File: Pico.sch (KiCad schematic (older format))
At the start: 5 parts, among them SW3001 SWITCH TACTILE SPST-NO 50MA 1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, U3001 Pico-JER

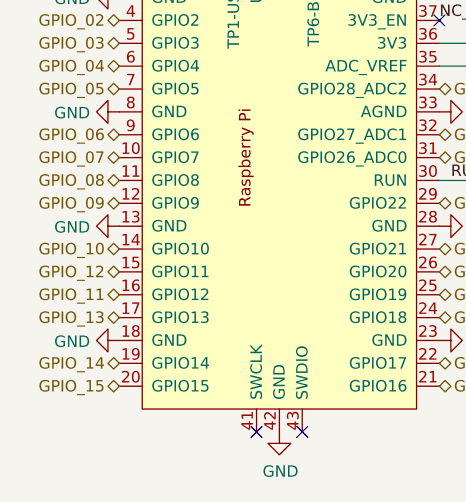
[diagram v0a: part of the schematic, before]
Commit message: Assignments for Pico GPIO 11 and 12 were flipped. Fixed.
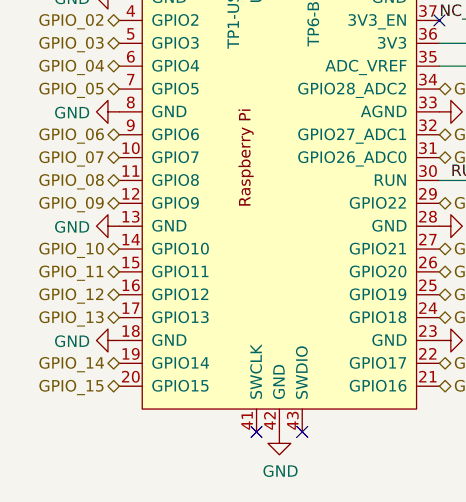
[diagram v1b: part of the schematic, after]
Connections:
- net GPIO_11: now also U3001.15 (GPIO11); no longer U3001.16 (GPIO12)
- net GPIO_12: now also U3001.16 (GPIO12); no longer U3001.15 (GPIO11)
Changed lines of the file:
@@
 GPIO_10
 Text HLabel 4900 4050 0    50   BiDi ~ 0
-GPIO_12
-Text HLabel 4900 4150 0    50   BiDi ~ 0
 GPIO_11
 Text HLabel 4900 4250 0    50   BiDi ~ 0
@@
 Text Label 6350 3650 0    50   ~ 0
 RUN_SW
+Text HLabel 4900 4150 0    50   BiDi ~ 0
+GPIO_12
 $EndSCHEMATC

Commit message: Use GP25_LED for ePaper RESET
Note: This replaces R6/196a722 in its entirety.

IS: J2901 (Connector for epaper) Pin 10 (Reset) connected to +3.3V via R2902 (100k ohm)
SHOULD BE: J2901 Pin 10 connected to U2801 Pin 48 (GPIO25_LED aka TP5)
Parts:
- U3001: symbol TMPCB_R2:Pico-JER -> TMPCB_R2:Pico-JER_no_usb_w_GP25
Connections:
- new net GPIO25_LED: U3001.48 (TP1-LED)
- no-connect marks 8 -> 4
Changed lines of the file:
@@
 $Descr A4 11693 8268
 encoding utf-8
-Sheet 30 30
+Sheet 19 30
 Title ""
 Date ""
@@
 	7500 3050 7500 2450
 Connection ~ 7500 3050
-$Comp
-L TMPCB_R2:Pico-JER U?
+NoConn ~ 6300 2750
+$Comp
+L Device:C_Small C3001
+U 1 1 61A6E1D1
+P 7500 3300
+F 0 "C3001" H 7592 3346 50  0000 L CNN
+F 1 "1 uF 10% 10V" H 7592 3255 50  0000 L CNN
+F 2 "Capacitor_SMD:C_0805_2012Metric_Pad1.18x1.45mm_HandSolder" H 7500 3300 50  0001 C CNN
+F 3 "http://www.samsungsem.com/kr/support/product-search/mlcc/CL21B105KPFNNNE.jsp" H 7500 3300 50  0001 C CNN
+F 4 "1276-1275-1-ND" H 7500 3300 50  0001 C CNN "Digikey PN"
+F 5 "Samsung Electro-Mechanics" H 7500 3300 50  0001 C CNN "MFG"
+F 6 "CL21B105KPFNNNE" H 7500 3300 50  0001 C CNN "MFG #"
+	1    7500 3300
+	1    0    0    -1
+$EndComp
+$Comp
+L Device:C_Small C3002
+U 1 1 61A6D580
+P 8200 3300
+F 0 "C3002" H 8292 3346 50  0000 L CNN
+F 1 "1 uF 10% 10V" H 8292 3255 50  0000 L CNN
+F 2 "Capacitor_SMD:C_0805_2012Metric_Pad1.18x1.45mm_HandSolder" H 8200 3300 50  0001 C CNN
+F 3 "http://www.samsungsem.com/kr/support/product-search/mlcc/CL21B105KPFNNNE.jsp" H 8200 3300 50  0001 C CNN
+F 4 "1276-1275-1-ND" H 8200 3300 50  0001 C CNN "Digikey PN"
+F 5 "Samsung Electro-Mechanics" H 8200 3300 50  0001 C CNN "MFG"
+F 6 "CL21B105KPFNNNE" H 8200 3300 50  0001 C CNN "MFG #"
+	1    8200 3300
+	1    0    0    -1
+$EndComp
+$Comp
+L Device:R_Small_US R3001
+U 1 1 61A781B3
+P 7900 4000
+F 0 "R3001" H 7968 4046 50  0000 L CNN
+F 1 "4.7k 5%" H 7968 3955 50  0000 L CNN
+F 2 "Resistor_SMD:R_0805_2012Metric_Pad1.20x1.40mm_HandSolder" H 7900 4000 50  0001 C CNN
+F 3 "https://www.seielect.com/catalog/sei-rmcf_rmcp.pdf" H 7900 4000 50  0001 C CNN
+F 4 "RMCF0805JT4K70CT-ND" H 7900 4000 50  0001 C CNN "Digikey PN"
+F 5 "Stackpole Electronics Inc" H 7900 4000 50  0001 C CNN "MFG"
+F 6 "RMCF0805JT4K70" H 7900 4000 50  0001 C CNN "MFG #"
+	1    7900 4000
+	1    0    0    -1
+$EndComp
+$Comp
+L power:+3V3 #PWR03012
+U 1 1 61A78C6E
+P 7900 3900
+F 0 "#PWR03012" H 7900 3750 50  0001 C CNN
+F 1 "+3V3" H 7915 4073 50  0000 C CNN
+F 2 "" H 7900 3900 50  0001 C CNN
+F 3 "" H 7900 3900 50  0001 C CNN
+	1    7900 3900
+	1    0    0    -1
+$EndComp
+Wire Wire Line
+	6300 3650 7200 3650
+Wire Wire Line
+	7200 3650 7200 4100
+Wire Wire Line
+	7200 4100 7900 4100
+$Comp
+L Switch:SW_Push SW3001
+U 1 1 61A7983A
+P 8750 4100
+F 0 "SW3001" H 8750 4385 50  0000 C CNN
+F 1 "SWITCH TACTILE SPST-NO 50MA 12V" H 8750 4294 50  0000 C CNN
+F 2 "Button_Switch_SMD:SW_SPST_TL3305A" H 8750 4300 50  0001 C CNN
+F 3 "https://sten-eswitch-13110800-production.s3.amazonaws.com/system/asset/product_line/data_sheet/213/TL3305.pdf" H 8750 4300 50  0001 C CNN
+F 4 "EG5353CT-ND" H 8750 4100 50  0001 C CNN "Digikey PN"
+F 5 "E-Switch" H 8750 4100 50  0001 C CNN "MFG"
+F 6 "TL3305AF260QG" H 8750 4100 50  0001 C CNN "MFG #"
+	1    8750 4100
+	1    0    0    -1
+$EndComp
+Wire Wire Line
+	7900 4100 8550 4100
+Connection ~ 7900 4100
+$Comp
+L power:GND #PWR03015
+U 1 1 61A79E42
+P 8950 4250
+F 0 "#PWR03015" H 8950 4000 50  0001 C CNN
+F 1 "GND" H 8955 4077 50  0000 C CNN
+F 2 "" H 8950 4250 50  0001 C CNN
+F 3 "" H 8950 4250 50  0001 C CNN
+	1    8950 4250
+	1    0    0    -1
+$EndComp
+Wire Wire Line
+	8950 4250 8950 4100
+NoConn ~ 5500 4750
+NoConn ~ 5700 4750
+$Comp
+L power:GND #PWR03006
+U 1 1 61A7AE09
+P 6300 3350
+F 0 "#PWR03006" H 6300 3100 50  0001 C CNN
+F 1 "GND" V 6305 3222 50  0000 R CNN
+F 2 "" H 6300 3350 50  0001 C CNN
+F 3 "" H 6300 3350 50  0001 C CNN
+	1    6300 3350
+	0    -1   -1   0
+$EndComp
+Wire Wire Line
+	8200 2450 8200 2650
+Wire Wire Line
+	6300 2650 8200 2650
+Connection ~ 8200 2650
+Wire Wire Line
+	8200 2650 8200 3200
+Wire Wire Line
+	6500 2850 6650 2850
+Wire Wire Line
+	6300 2850 6500 2850
+Connection ~ 6500 2850
+$Comp
+L power:PWR_FLAG #FLG03001
+U 1 1 61A20D92
+P 6500 2850
+F 0 "#FLG03001" H 6500 2925 50  0001 C CNN
+F 1 "PWR_FLAG" H 6500 3023 50  0000 C CNN
+F 2 "" H 6500 2850 50  0001 C CNN
+F 3 "~" H 6500 2850 50  0001 C CNN
+	1    6500 2850
+	1    0    0    -1
+$EndComp
+Text Label 6300 2750 0    50   ~ 0
+NC_VSYS
+Text Label 6300 2950 0    50   ~ 0
+NC_3V3_EN
+Text Label 6350 3650 0    50   ~ 0
+RUN_SW
+Text HLabel 4900 4150 0    50   BiDi ~ 0
+GPIO_12
+Text HLabel 5900 2450 1    50   Input ~ 0
+GPIO25_LED
+$Comp
+L TMPCB_R2:Pico-JER_no_usb_w_GP25 U?
 U 1 1 61A62316
 P 5600 3600
@@
 	1    0    0    -1
 $EndComp
-NoConn ~ 6300 2750
-$Comp
-L Device:C_Small C3001
-U 1 1 61A6E1D1
-P 7500 3300
-F 0 "C3001" H 7592 3346 50  0000 L CNN
-F 1 "1 uF 10% 10V" H 7592 3255 50  0000 L CNN
-F 2 "Capacitor_SMD:C_0805_2012Metric_Pad1.18x1.45mm_HandSolder" H 7500 3300 50  0001 C CNN
-F 3 "http://www.samsungsem.com/kr/support/product-search/mlcc/CL21B105KPFNNNE.jsp" H 7500 3300 50  0001 C CNN
-F 4 "1276-1275-1-ND" H 7500 3300 50  0001 C CNN "Digikey PN"
-F 5 "Samsung Electro-Mechanics" H 7500 3300 50  0001 C CNN "MFG"
-F 6 "CL21B105KPFNNNE" H 7500 3300 50  0001 C CNN "MFG #"
-	1    7500 3300
-	1    0    0    -1
-$EndComp
-$Comp
-L Device:C_Small C3002
-U 1 1 61A6D580
-P 8200 3300
-F 0 "C3002" H 8292 3346 50  0000 L CNN
-F 1 "1 uF 10% 10V" H 8292 3255 50  0000 L CNN
-F 2 "Capacitor_SMD:C_0805_2012Metric_Pad1.18x1.45mm_HandSolder" H 8200 3300 50  0001 C CNN
-F 3 "http://www.samsungsem.com/kr/support/product-search/mlcc/CL21B105KPFNNNE.jsp" H 8200 3300 50  0001 C CNN
-F 4 "1276-1275-1-ND" H 8200 3300 50  0001 C CNN "Digikey PN"
-F 5 "Samsung Electro-Mechanics" H 8200 3300 50  0001 C CNN "MFG"
-F 6 "CL21B105KPFNNNE" H 8200 3300 50  0001 C CNN "MFG #"
-	1    8200 3300
-	1    0    0    -1
-$EndComp
-$Comp
-L Device:R_Small_US R3001
-U 1 1 61A781B3
-P 7900 4000
-F 0 "R3001" H 7968 4046 50  0000 L CNN
-F 1 "4.7k 5%" H 7968 3955 50  0000 L CNN
-F 2 "Resistor_SMD:R_0805_2012Metric_Pad1.20x1.40mm_HandSolder" H 7900 4000 50  0001 C CNN
-F 3 "https://www.seielect.com/catalog/sei-rmcf_rmcp.pdf" H 7900 4000 50  0001 C CNN
-F 4 "RMCF0805JT4K70CT-ND" H 7900 4000 50  0001 C CNN "Digikey PN"
-F 5 "Stackpole Electronics Inc" H 7900 4000 50  0001 C CNN "MFG"
-F 6 "RMCF0805JT4K70" H 7900 4000 50  0001 C CNN "MFG #"
-	1    7900 4000
-	1    0    0    -1
-$EndComp
-$Comp
-L power:+3V3 #PWR03012
-U 1 1 61A78C6E
-P 7900 3900
-F 0 "#PWR03012" H 7900 3750 50  0001 C CNN
-F 1 "+3V3" H 7915 4073 50  0000 C CNN
-F 2 "" H 7900 3900 50  0001 C CNN
-F 3 "" H 7900 3900 50  0001 C CNN
-	1    7900 3900
-	1    0    0    -1
-$EndComp
-Wire Wire Line
-	6300 3650 7200 3650
-Wire Wire Line
-	7200 3650 7200 4100
-Wire Wire Line
-	7200 4100 7900 4100
-$Comp
-L Switch:SW_Push SW3001
-U 1 1 61A7983A
-P 8750 4100
-F 0 "SW3001" H 8750 4385 50  0000 C CNN
-F 1 "SWITCH TACTILE SPST-NO 50MA 12V" H 8750 4294 50  0000 C CNN
-F 2 "Button_Switch_SMD:SW_SPST_TL3305A" H 8750 4300 50  0001 C CNN
-F 3 "https://sten-eswitch-13110800-production.s3.amazonaws.com/system/asset/product_line/data_sheet/213/TL3305.pdf" H 8750 4300 50  0001 C CNN
-F 4 "EG5353CT-ND" H 8750 4100 50  0001 C CNN "Digikey PN"
-F 5 "E-Switch" H 8750 4100 50  0001 C CNN "MFG"
-F 6 "TL3305AF260QG" H 8750 4100 50  0001 C CNN "MFG #"
-	1    8750 4100
-	1    0    0    -1
-$EndComp
-Wire Wire Line
-	7900 4100 8550 4100
-Connection ~ 7900 4100
-$Comp
-L power:GND #PWR03015
-U 1 1 61A79E42
-P 8950 4250
-F 0 "#PWR03015" H 8950 4000 50  0001 C CNN
-F 1 "GND" H 8955 4077 50  0000 C CNN
-F 2 "" H 8950 4250 50  0001 C CNN
-F 3 "" H 8950 4250 50  0001 C CNN
-	1    8950 4250
-	1    0    0    -1
-$EndComp
-Wire Wire Line
-	8950 4250 8950 4100
-NoConn ~ 5400 2450
-NoConn ~ 5500 2450
-NoConn ~ 5600 2450
-NoConn ~ 5750 2450
-NoConn ~ 5500 4750
-NoConn ~ 5700 4750
-$Comp
-L power:GND #PWR03006
-U 1 1 61A7AE09
-P 6300 3350
-F 0 "#PWR03006" H 6300 3100 50  0001 C CNN
-F 1 "GND" V 6305 3222 50  0000 R CNN
-F 2 "" H 6300 3350 50  0001 C CNN
-F 3 "" H 6300 3350 50  0001 C CNN
-	1    6300 3350
-	0    -1   -1   0
-$EndComp
-Wire Wire Line
-	8200 2450 8200 2650
-Wire Wire Line
-	6300 2650 8200 2650
-Connection ~ 8200 2650
-Wire Wire Line
-	8200 2650 8200 3200
-Wire Wire Line
-	6500 2850 6650 2850
-Wire Wire Line
-	6300 2850 6500 2850
-Connection ~ 6500 2850
-$Comp
-L power:PWR_FLAG #FLG03001
-U 1 1 61A20D92
-P 6500 2850
-F 0 "#FLG03001" H 6500 2925 50  0001 C CNN
-F 1 "PWR_FLAG" H 6500 3023 50  0000 C CNN
-F 2 "" H 6500 2850 50  0001 C CNN
-F 3 "~" H 6500 2850 50  0001 C CNN
-	1    6500 2850
-	1    0    0    -1
-$EndComp
-Text Label 6300 2750 0    50   ~ 0
-NC_VSYS
-Text Label 6300 2950 0    50   ~ 0
-NC_3V3_EN
-Text Label 6350 3650 0    50   ~ 0
-RUN_SW
-Text HLabel 4900 4150 0    50   BiDi ~ 0
-GPIO_12
 $EndSCHEMATC
